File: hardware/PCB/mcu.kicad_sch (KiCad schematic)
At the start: 0 parts

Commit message: drawings
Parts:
- added U2: STM32H747IITx, Package_QFP:LQFP-176_24x24mm_P0.5mm, symbol MCU_ST_STM32H7:STM32H747IITx
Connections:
- new net: U2.100 (VSS), U2.112 (VSS), U2.119 (VSS), U2.12 (VSS), U2.134 (VSS), U2.137 (VSS), U2.151 (VSS), U2.159 (VSS), U2.173 (VSS), U2.24 (VSS), U2.45 (VSS), U2.47 (VSS), U2.6 (VSS), U2.64 (VSS), U2.70 (VSS), U2.81 (VSS), U2.83 (VSS), U2.93 (VSS)
- new net: U2.105 (VSSDSI), U2.109 (VSSDSI)

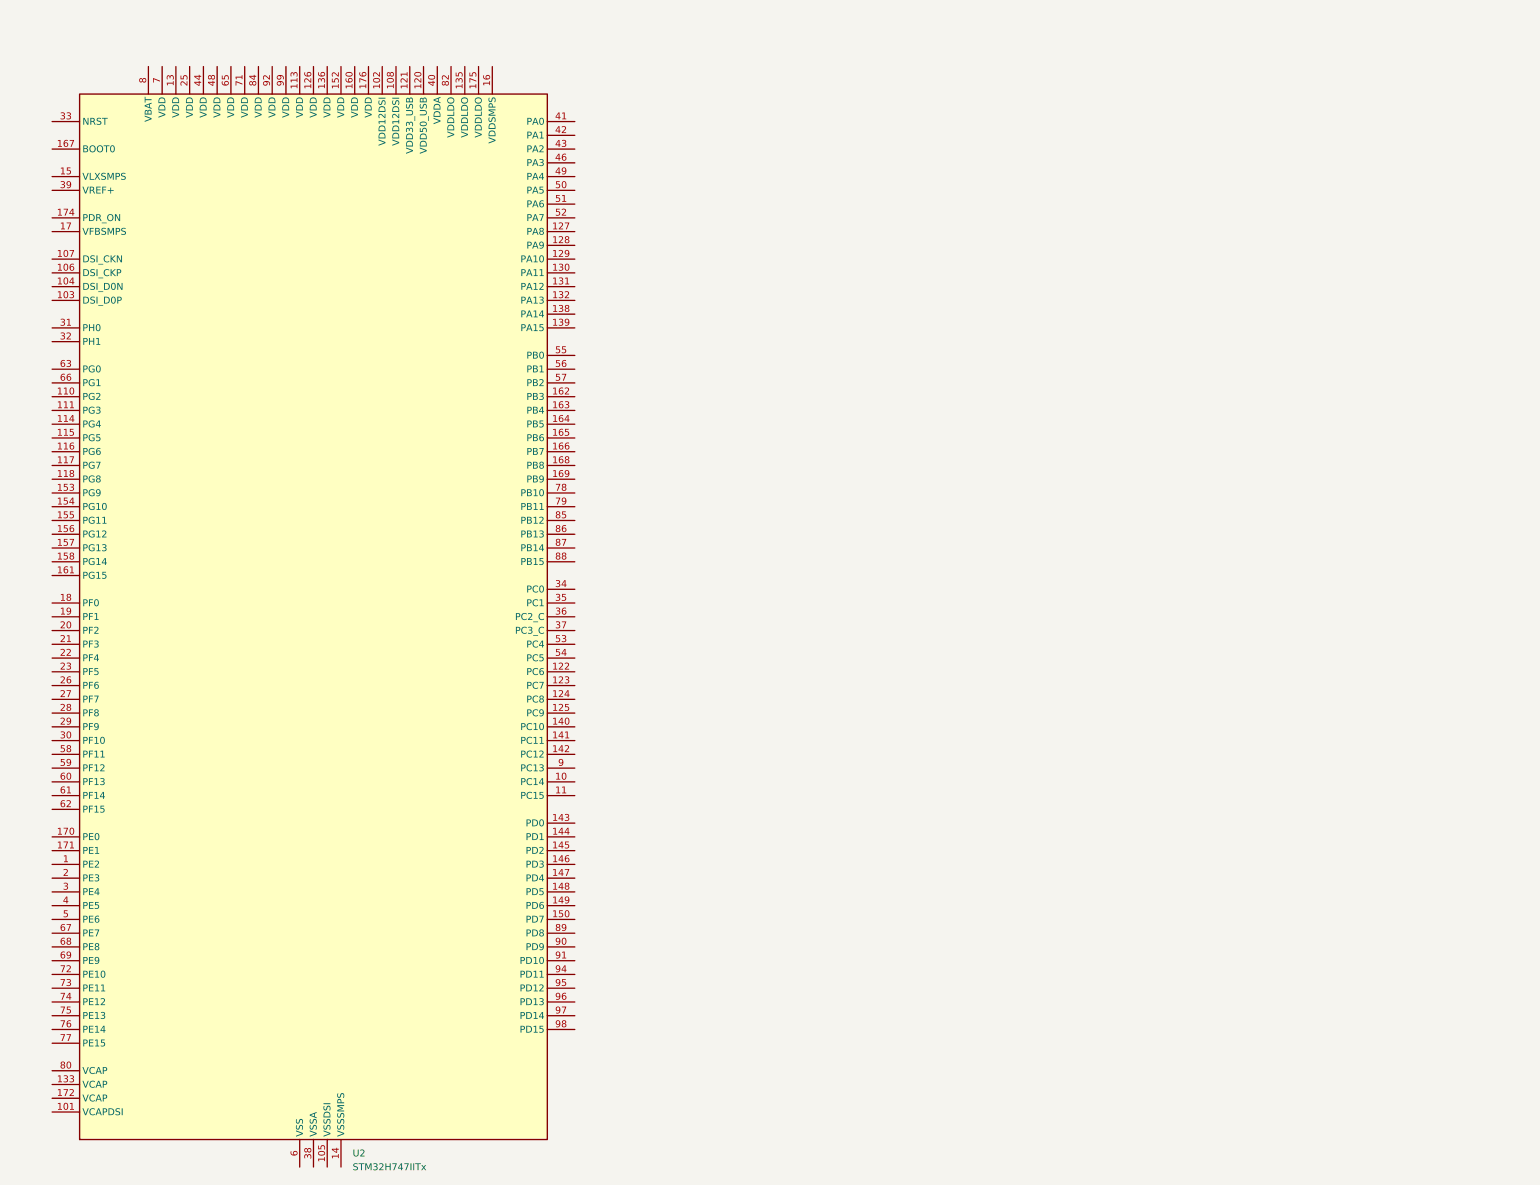
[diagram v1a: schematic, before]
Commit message: lcd pin connections
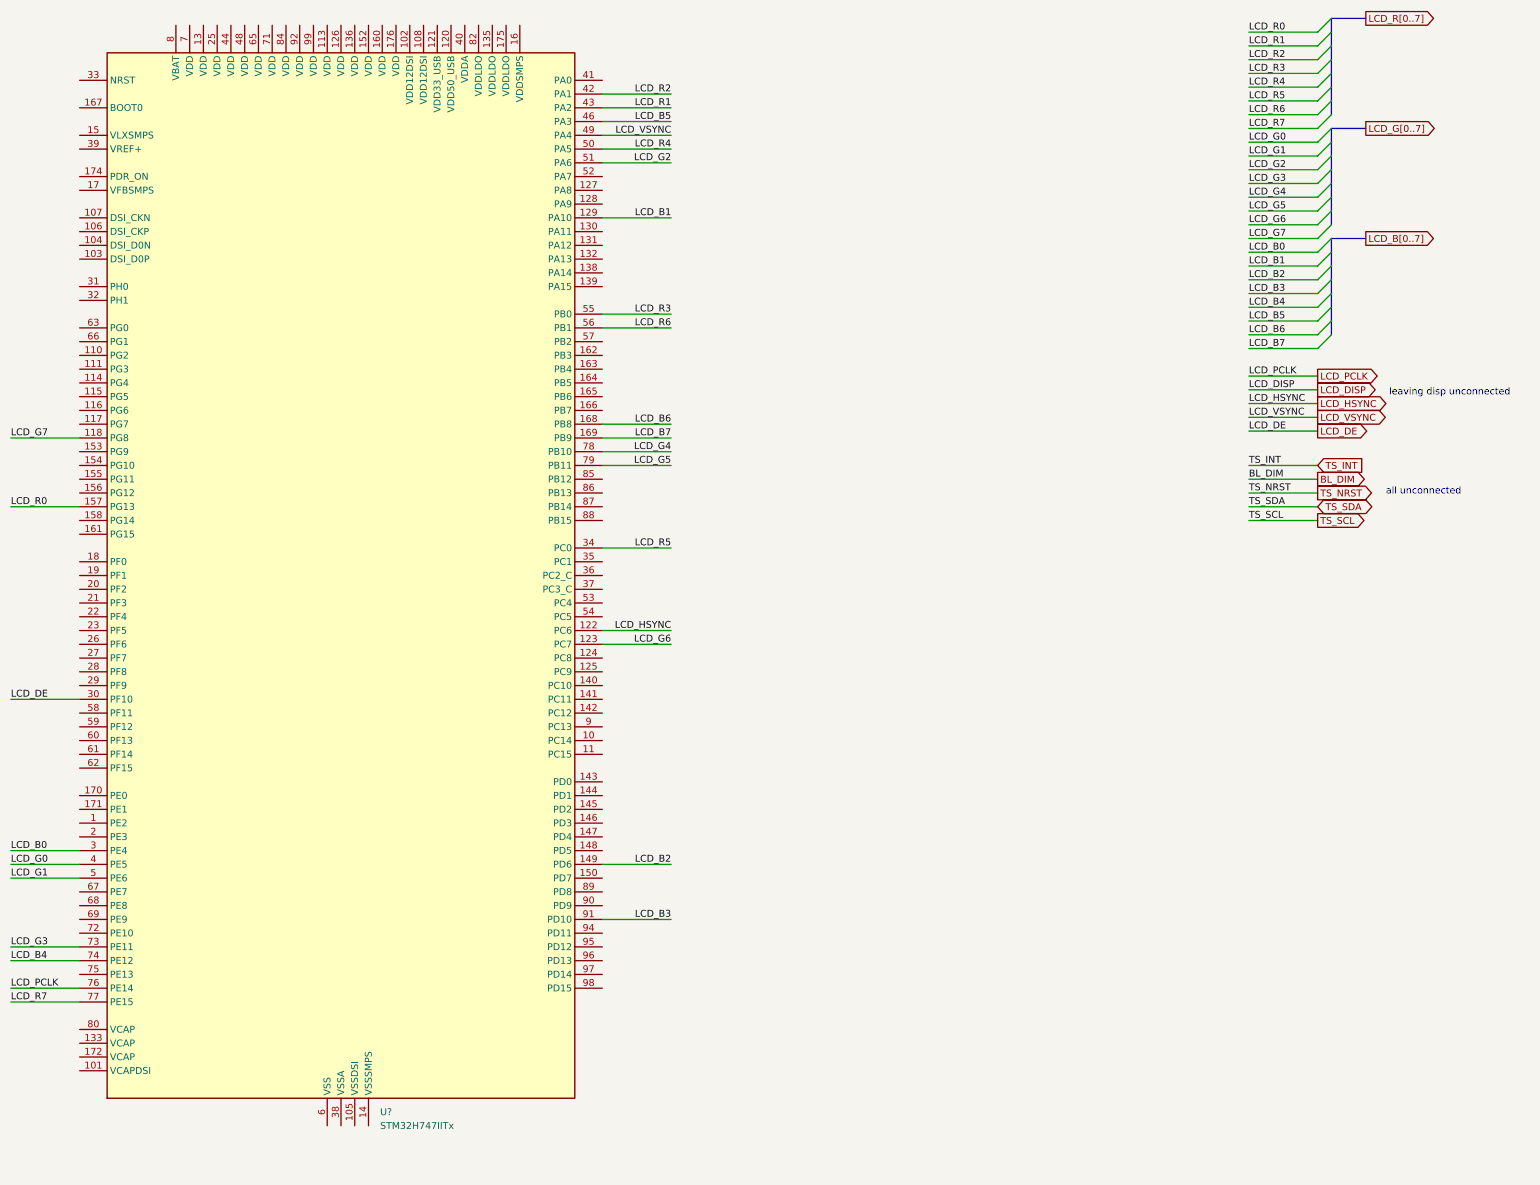
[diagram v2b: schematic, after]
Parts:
- renumbered U2 to U?
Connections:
- net LCD_G7: now reaches U?.118 (PG8)
- net LCD_HSYNC: now reaches U?.122 (PC6)
- net LCD_G6: now reaches U?.123 (PC7)
- net LCD_B1: now reaches U?.129 (PA10)
- net LCD_B2: now reaches U?.149 (PD6)
- net LCD_R0: now reaches U?.157 (PG13)
- net LCD_B6: now reaches U?.168 (PB8)
- net LCD_B7: now reaches U?.169 (PB9)
- net LCD_B0: now reaches U?.3 (PE4)
- net LCD_DE: now reaches U?.30 (PF10)
- net LCD_R5: now reaches U?.34 (PC0)
- net LCD_G0: now reaches U?.4 (PE5)
- net LCD_R2: now reaches U?.42 (PA1)
- net LCD_R1: now reaches U?.43 (PA2)
- net LCD_B5: now reaches U?.46 (PA3)
- net LCD_VSYNC: now reaches U?.49 (PA4)
- net LCD_G1: now reaches U?.5 (PE6)
- net LCD_R4: now reaches U?.50 (PA5)
- net LCD_G2: now reaches U?.51 (PA6)
- net LCD_R3: now reaches U?.55 (PB0)
- net LCD_R6: now reaches U?.56 (PB1)
- net LCD_G3: now reaches U?.73 (PE11)
- net LCD_B4: now reaches U?.74 (PE12)
- net LCD_PCLK: now reaches U?.76 (PE14)
- net LCD_R7: now reaches U?.77 (PE15)
- net LCD_G4: now reaches U?.78 (PB10)
- net LCD_G5: now reaches U?.79 (PB11)
- net LCD_B3: now reaches U?.91 (PD10)
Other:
- note added: "all unconnected"
- note added: "leaving disp unconnected"
- moved on the sheet: U?

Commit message: debounce
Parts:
- added C5, C6: 1u, symbol Device:C
- added R14, R15: 10k, symbol Device:R_US
- added SW1: RESET, symbol Switch:SW_Push
- added SW2: PROG, symbol Switch:SW_Push
- gave numbers to parts that had none: 1
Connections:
- net NOR_D2: now reaches U2.1 (PE2)
- net NOR_CS: now reaches U2.116 (PG6)
- net SD_D0: now reaches U2.124 (PC8)
- net SD_D1: now reaches U2.125 (PC9)
- net USB_VBUS: now reaches U2.128 (PA9)
- net USB_DM: now reaches U2.130 (PA11)
- net USB_DP: now reaches U2.131 (PA12)
- net SD_D2: now reaches U2.140 (PC10)
- net SD_D3: now reaches U2.141 (PC11)
- net SD_CLK: now reaches U2.142 (PC12)
- net SD_CMD: now reaches U2.145 (PD2)
- net PROG: now reaches U2.167 (BOOT0)
- net PROG: now also C6.1, R14.1, SW2.1
- net NOR_D3: now reaches U2.26 (PF6)
- net NOR_D0: now reaches U2.28 (PF8)
- net NOR_D1: now reaches U2.29 (PF9)
- net RESET: now reaches U2.33 (NRST)
- net RESET: now also C5.1, R15.2, SW1.1
- net NOR_CLK: now reaches U2.57 (PB2)
- new net +3.3V: R15.1, SW2.2
- new net GND: C5.2, C6.2, R14.2, SW1.2
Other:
- note added: "CD unconnected"

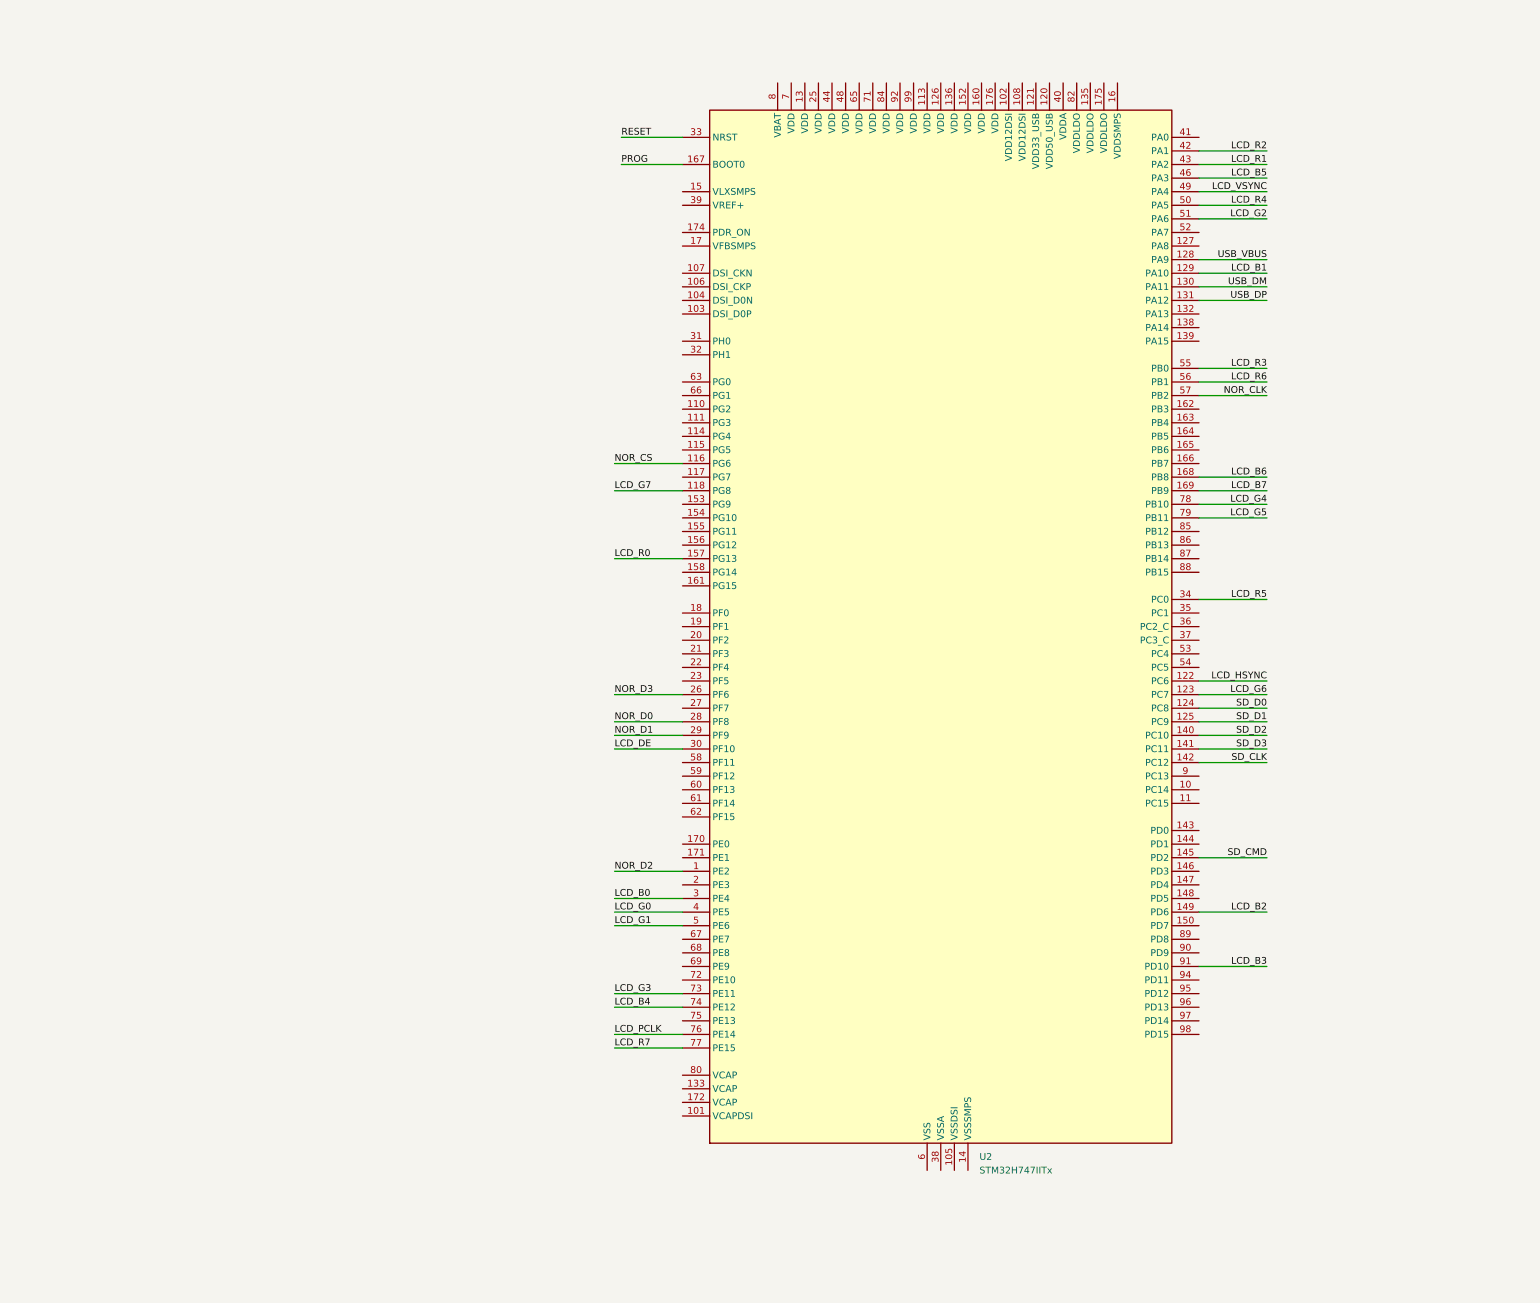
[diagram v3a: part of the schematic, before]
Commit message: Update MCU
Decoupling caps
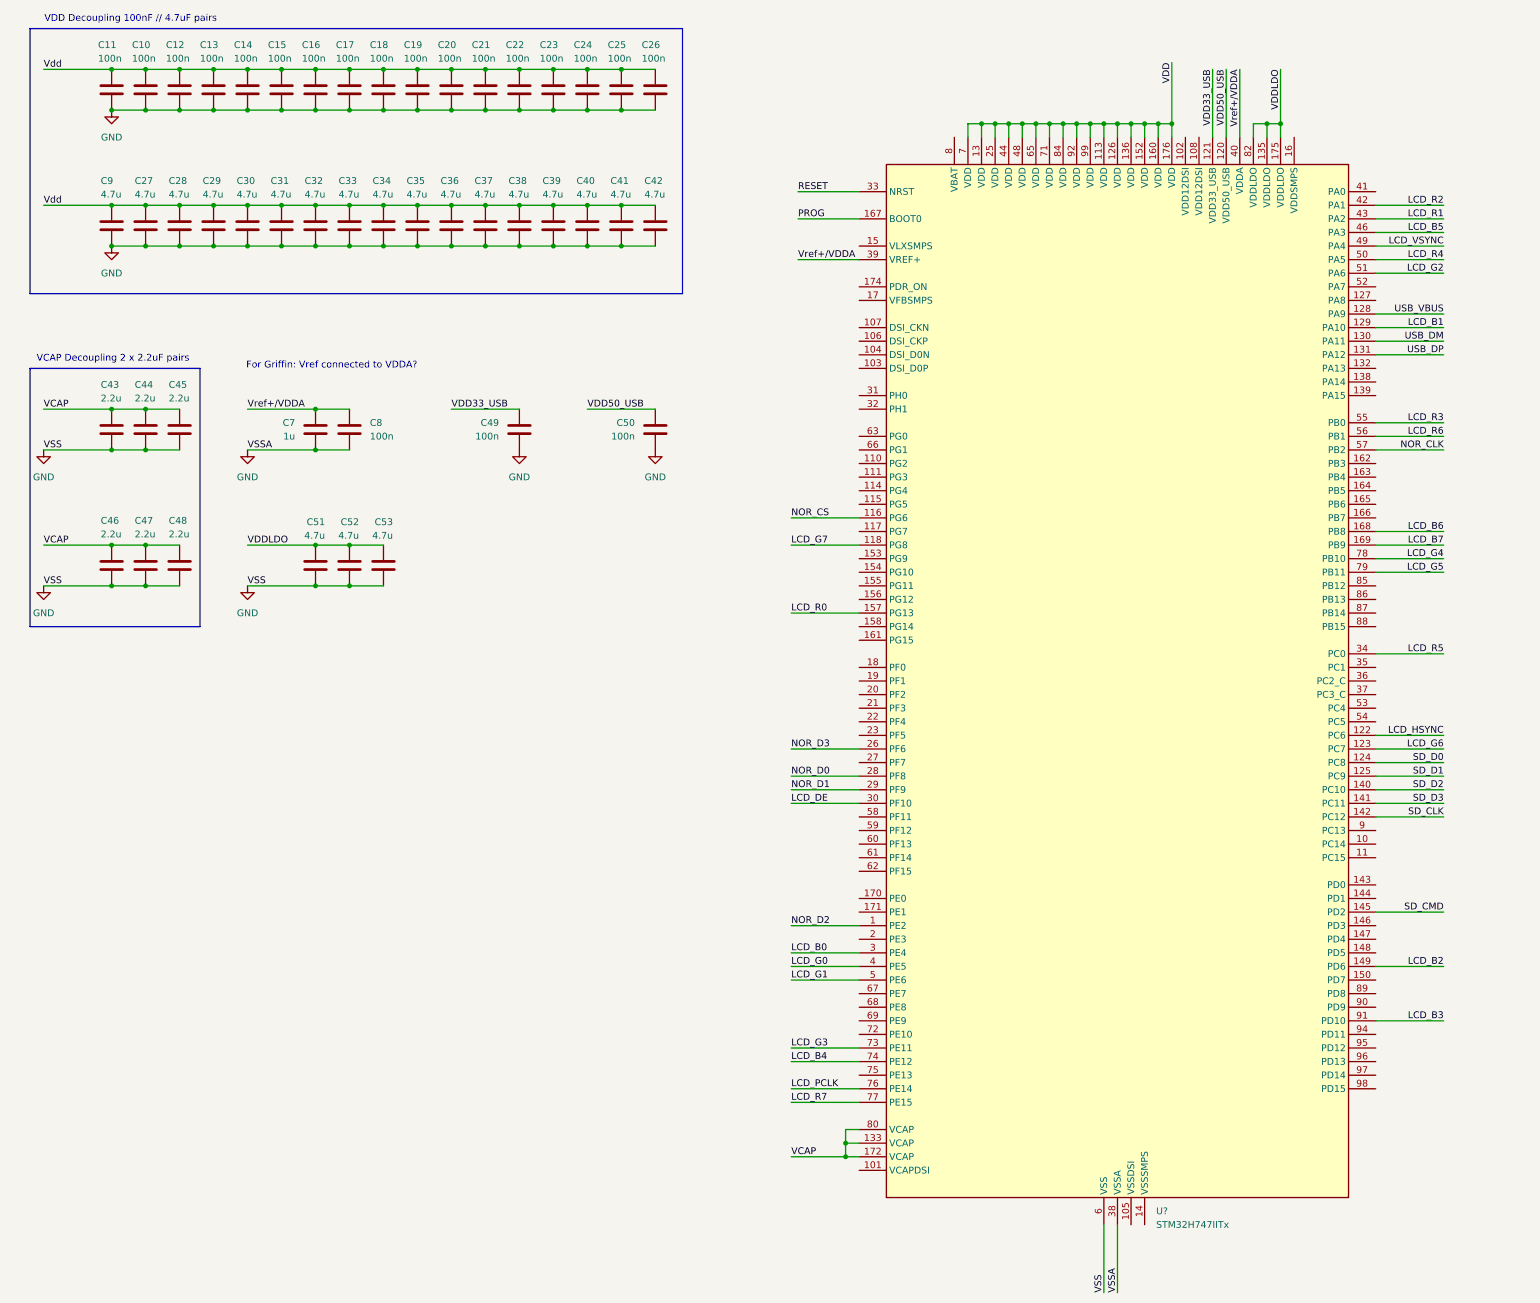
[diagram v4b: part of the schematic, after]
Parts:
- added C10, C11, C12, C13, C14, C15, C16, C17, C18, C19, C20, C21, C22, C23, C24, C25, C26, C49, C50, C8: 100n, symbol Device:C
- added C27, C28, C29, C30, C31, C32, C33, C34, C35, C36, C37, C38, C39, C40, C41, C42, C51, C52, C53, C9: 4.7u, symbol Device:C
- added C43, C44, C45, C46, C47, C48: 2.2u, symbol Device:C
- added C7: 1u, symbol Device:C
- renumbered U2 to U?
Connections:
- net GND: now also U?.100 (VSS), U?.112 (VSS), U?.119 (VSS), U?.12 (VSS), U?.134 (VSS), U?.137 (VSS), U?.151 (VSS), U?.159 (VSS), U?.173 (VSS), U?.24 (VSS), U?.38 (VSSA), U?.45 (VSS), U?.47 (VSS), U?.6 (VSS), U?.64 (VSS), U?.70 (VSS), U?.81 (VSS), U?.83 (VSS), U?.93 (VSS), C10.2, C11.2, C12.2, C13.2, C14.2, C15.2, C16.2, C17.2, C18.2, C19.2, C20.2, C21.2, C22.2, C23.2, C24.2, C25.2, C26.2, C27.2, C28.2, C29.2, C30.2, C31.2, C32.2, C33.2, C34.2, C35.2, C36.2, C37.2, C38.2, C39.2, C40.2, C41.2, C42.2, C43.2, C44.2, C45.2, C46.2, C47.2, C48.2, C49.2, C50.2, C51.2, C52.2, C53.2, C7.2, C8.2, C9.2
- net VDD: now reaches U?.113 (VDD)
- net VDD: now also U?.126 (VDD), U?.13 (VDD), U?.136 (VDD), U?.152 (VDD), U?.160 (VDD), U?.176 (VDD), U?.25 (VDD), U?.44 (VDD), U?.48 (VDD), U?.65 (VDD), U?.7 (VDD), U?.71 (VDD), U?.84 (VDD), U?.92 (VDD), U?.99 (VDD)
- net VDD50_USB: now reaches U?.120 (VDD50_USB)
- net VDD50_USB: now also C50.1
- net VDD33_USB: now reaches U?.121 (VDD33_USB)
- net VDD33_USB: now also C49.1
- net VCAP: now reaches U?.133 (VCAP)
- net VCAP: now also U?.172 (VCAP), U?.80 (VCAP), C43.1, C44.1, C45.1, C46.1, C47.1, C48.1
- net VDDLDO: now reaches U?.135 (VDDLDO)
- net VDDLDO: now also U?.175 (VDDLDO), U?.82 (VDDLDO), C51.1, C52.1, C53.1
- net Vref+/VDDA: now reaches U?.39 (VREF+)
- net Vref+/VDDA: now also U?.40 (VDDA), C7.1, C8.1
- new net Vdd: C10.1, C11.1, C12.1, C13.1, C14.1, C15.1, C16.1, C17.1, C18.1, C19.1, C20.1, C21.1, C22.1, C23.1, C24.1, C25.1, C26.1, C27.1, C28.1, C29.1, C30.1, C31.1, C32.1, C33.1, C34.1, C35.1, C36.1, C37.1, C38.1, C39.1, C40.1, C41.1, C42.1, C9.1
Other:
- note added: "For Griffin: Vref connected to VDDA?"
- note added: "VCAP Decoupling 2 x 2.2uF pairs"
- note added: "VDD Decoupling 100nF // 4.7uF pairs"
- moved on the sheet: U?

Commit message: Update mcu
redone decoupling caps
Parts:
- removed C28, C29, C30, C31, C32, C33, C34, C35, C36, C37, C38, C39, C40, C41, C42, C52, C53: 4.7u, symbol Device:C
- removed C44, C45, C47, C48: 2.2u, symbol Device:C
- added J2: Conn_02x05_Odd_Even, symbol Connector_Generic:Conn_02x05_Odd_Even
- C27: value 4.7u -> 100n
- C50: value 100n -> 1u
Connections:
- net VDD is gone; now on net +3.3V: U?.113 (VDD), U?.126 (VDD), U?.13 (VDD), U?.136 (VDD), U?.152 (VDD), U?.160 (VDD), U?.176 (VDD), U?.25 (VDD), U?.44 (VDD), U?.48 (VDD), U?.65 (VDD), U?.7 (VDD), U?.71 (VDD), U?.84 (VDD), U?.92 (VDD), U?.99 (VDD)
- net VDD33_USB is gone; now on net +3.3V: C49.1, U?.121 (VDD33_USB)
- net VDD50_USB is gone; now on net +3.3V: C50.1, U?.120 (VDD50_USB)
- net VDDLDO is gone; now on net +3.3V: C51.1, U?.135 (VDDLDO), U?.175 (VDDLDO), U?.82 (VDDLDO)
- net Vref+/VDDA is gone; now on net +3.3V: C7.1, C8.1, U?.39 (VREF+), U?.40 (VDDA)
- net +3.3V: now also C10.1, C11.1, C12.1, C13.1, C14.1, C15.1, C16.1, C17.1, C18.1, C19.1, C20.1, C21.1, C22.1, C23.1, C24.1, C25.1, C26.1, C9.1, U?.174 (PDR_ON), U?.8 (VBAT)
- net GND: now also U?.105 (VSSDSI), U?.109 (VSSDSI), U?.14 (VSSSMPS), U?.16 (VDDSMPS), U?.17 (VFBSMPS), J2.3 (Pin_3), J2.4 (Pin_4)
- net RESET: now also J2.1 (Pin_1)
- net VCAPDSI: now reaches U?.101 (VCAPDSI)
- net VCAPDSI: now also U?.102 (VDD12DSI), U?.108 (VDD12DSI)
- removed net Vdd: C10.1, C11.1, C12.1, C13.1, C14.1, C15.1, C16.1, C17.1, C18.1, C19.1, C20.1, C21.1, C22.1, C23.1, C24.1, C25.1, C26.1, C27.1, C9.1
- new net SWCLK: J2.6 (Pin_6)
- new net SWDIO: J2.2 (Pin_2)
- new net VBAT: C27.1
- no-connect marks 0 -> 9
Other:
- note added: "Progrommer header"
- note added: "VCAP Decoupling 2 x 2.2uF pair"
- note added: "VDD Decoupling 100nF + 4.7uF"
- note added: "leaving disp unconnected until we decide gpio"
- note added: "test point/header for analog pins"
- note removed: "For Griffin: Vref connected to VDDA?"
- note removed: "VCAP Decoupling 2 x 2.2uF pairs"
- note removed: "VDD Decoupling 100nF // 4.7uF pairs"
- note removed: "leaving disp unconnected"
- moved on the sheet: C43, C46, C49, C50, C51, C7, C8, C9, U?

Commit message: mcu and top level update
more caps and mounting holes
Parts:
- added C28, C29, C30, C31: C, symbol Device:C
- added R16: R, symbol Device:R_US
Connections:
- net VBAT is gone; now on net +3.3V: C27.1
- net GND: now also C28.1, C29.2, C30.1, C31.2
- net OSC32_IN: now reaches U?.10 (PC14)
- net OSC32_IN: now also C30.2
- net OSC32_OUT: now reaches U?.11 (PC15)
- net OSC32_OUT: now also C31.1
- net OSC_IN: now reaches U?.31 (PH0)
- net OSC_IN: now also C28.2
- net OSC_OUT: now reaches U?.32 (PH1)
- net OSC_OUT: now also R16.2
- new net: C29.1, R16.1
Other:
- note added: "Analog Decoupling"
- note added: "Battery Decoupling"
- note added: "Debounce Circuits"
- note added: "LDO Supply Configuration Decoupling"
- note added: "To LCD"
- note added: "To STORAGE"
- note added: "USB Decoupling"
- note added: "VDD Decoupling"
- note removed: "VCAP Decoupling 2 x 2.2uF pair"
- note removed: "VDD Decoupling 100nF + 4.7uF"
- moved on the sheet: C27, C51, C7, C8, J2
